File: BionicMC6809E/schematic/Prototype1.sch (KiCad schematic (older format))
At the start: 5 parts, among them J1 BionicConnector, U1 MC6809P, U2 74HCT126

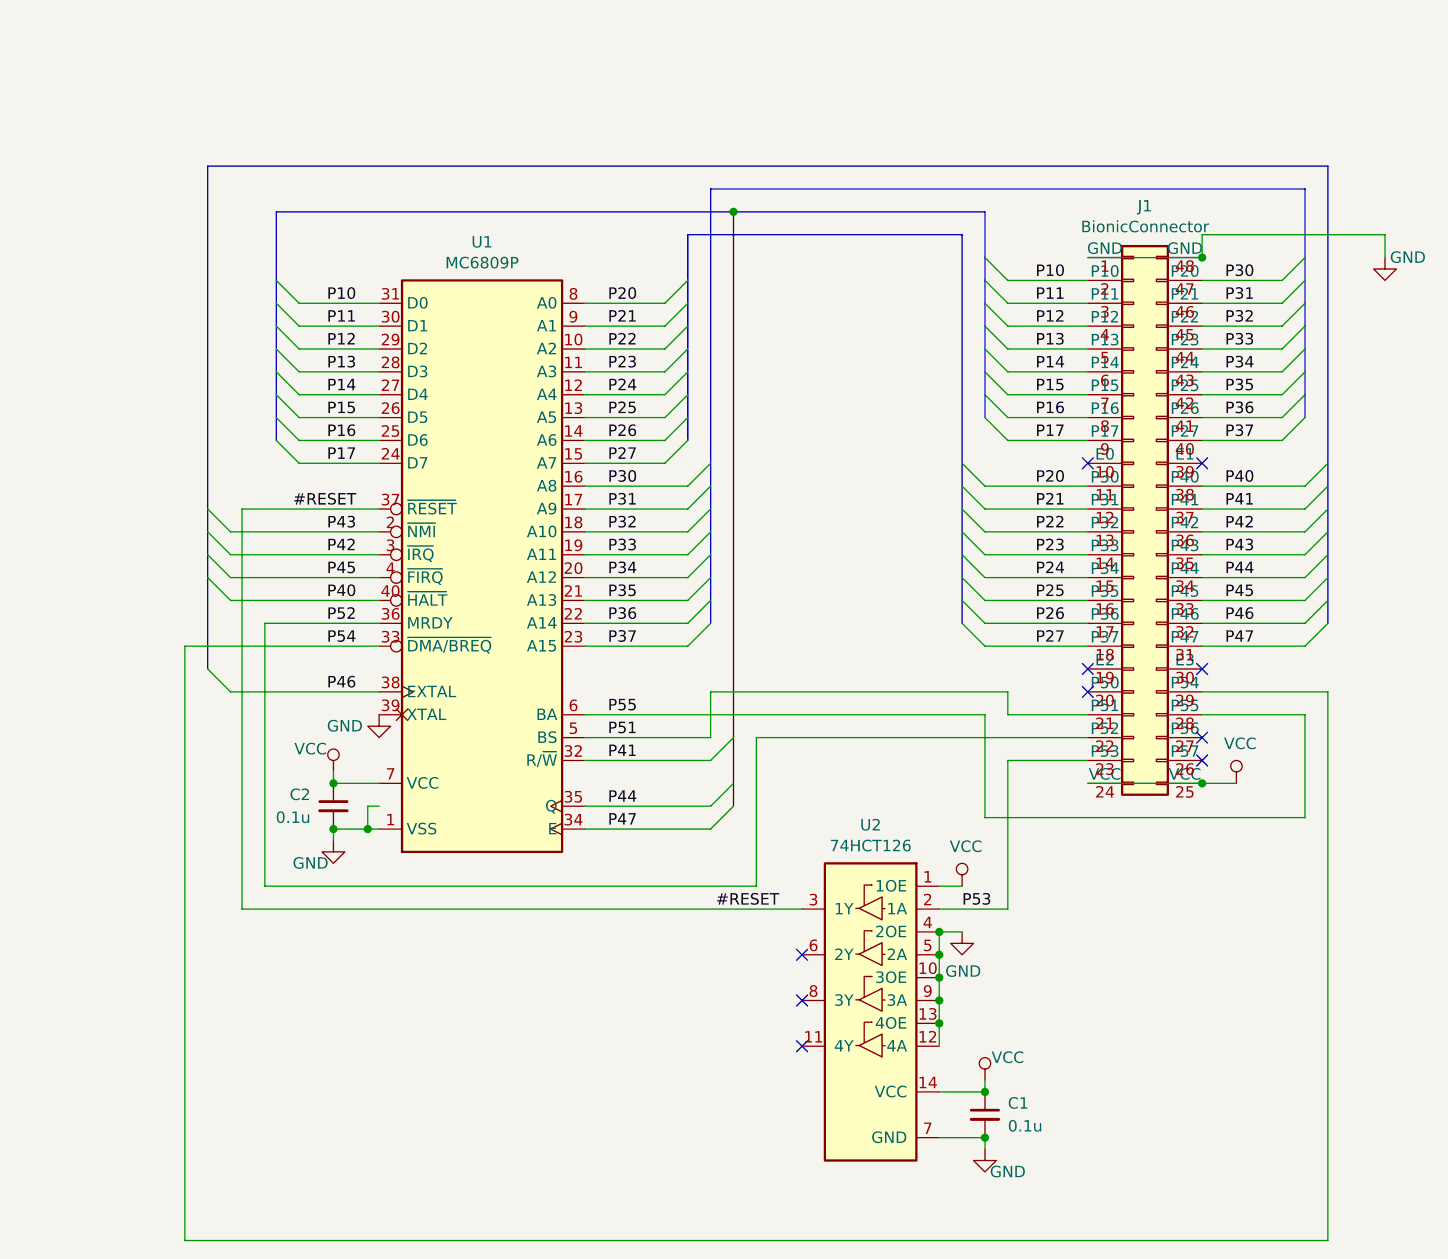
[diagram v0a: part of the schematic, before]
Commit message: [BionicMC6809E] Mezzanine board
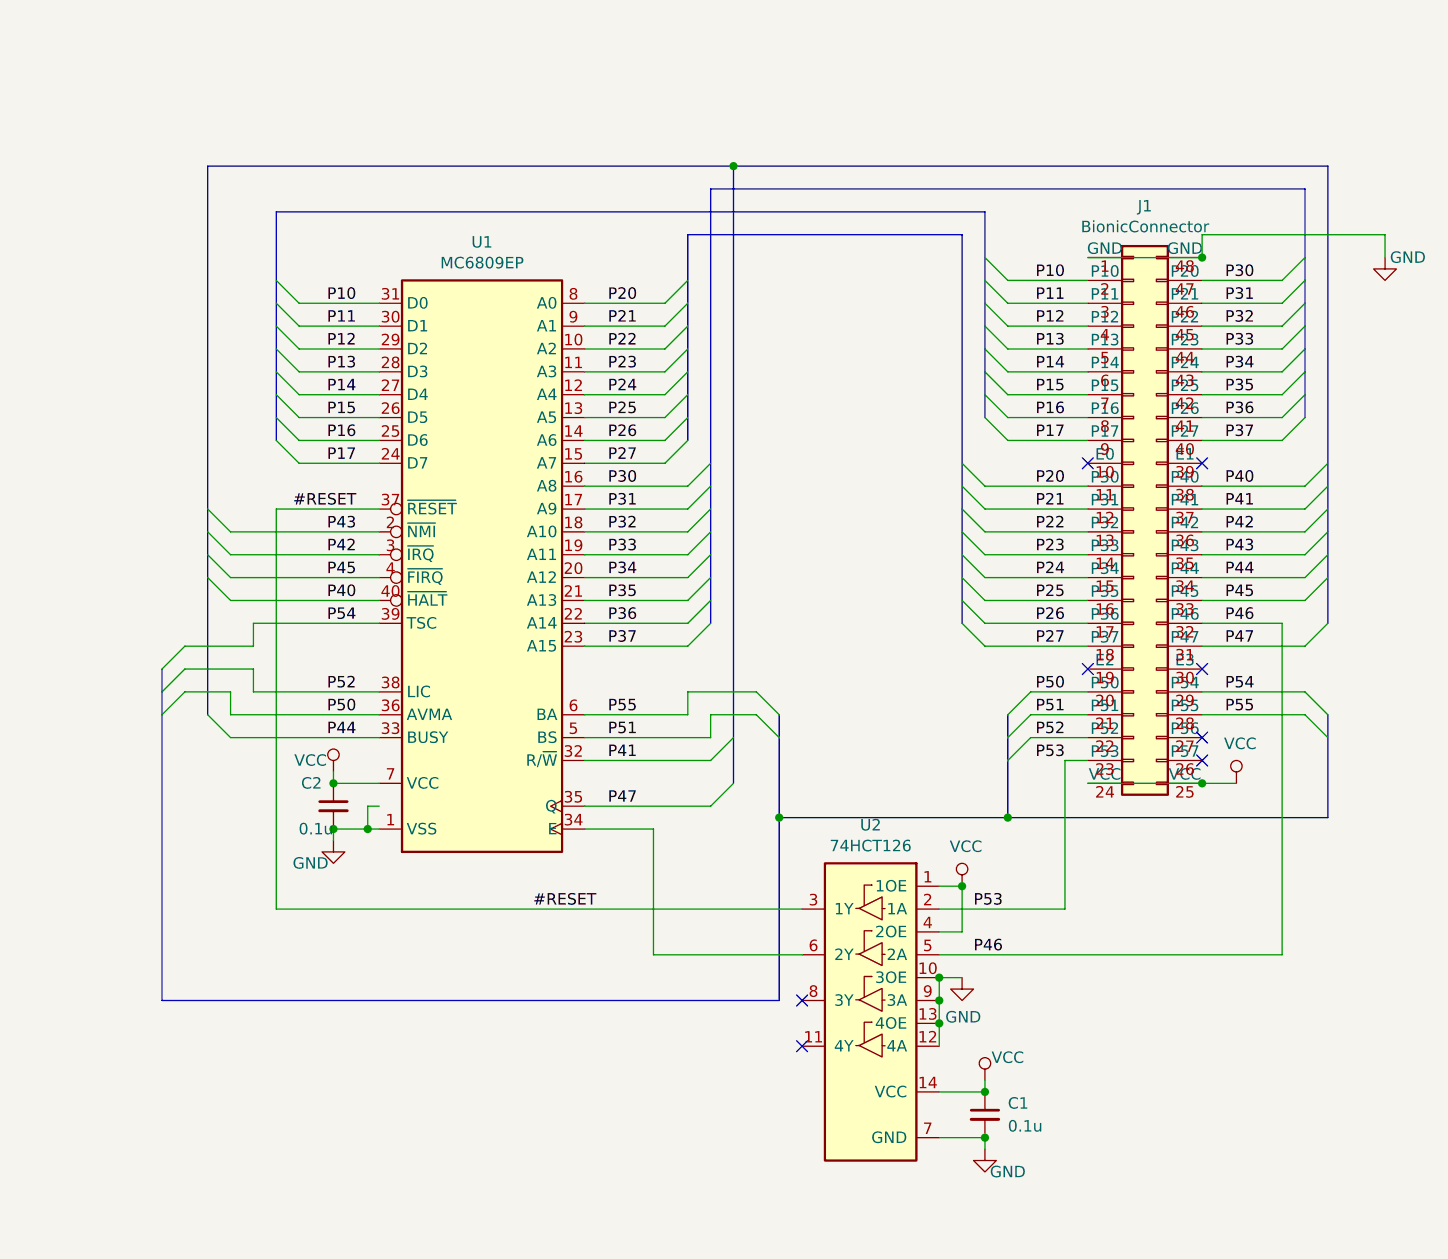
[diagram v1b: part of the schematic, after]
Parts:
- removed U1: MC6809P, Package_DIP:DIP-40_W15.24mm, symbol 0-LocalLibrary:MC6809P
- added U1: MC6809EP, Package_DIP:DIP-40_W15.24mm, symbol 0-LocalLibrary:MC6809EP
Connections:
- net #RESET: now also U1.37 (~RESET)
- net GND: now also U1.1 (VSS); no longer U2.4 (2OE), U2.5 (2A)
- net P10: now also U1.31 (D0)
- net P11: now also U1.30 (D1)
- net P12: now also U1.29 (D2)
- net P13: now also U1.28 (D3)
- net P14: now also U1.27 (D4)
- net P15: now also U1.26 (D5)
- net P16: now also U1.25 (D6)
- net P17: now also U1.24 (D7)
- net P20: now also U1.8 (A0)
- net P21: now also U1.9 (A1)
- net P22: now also U1.10 (A2)
- net P23: now also U1.11 (A3)
- net P24: now also U1.12 (A4)
- net P25: now also U1.13 (A5)
- net P26: now also U1.14 (A6)
- net P27: now also U1.15 (A7)
- net P30: now also U1.16 (A8)
- net P31: now also U1.17 (A9)
- net P32: now also U1.18 (A10)
- net P33: now also U1.19 (A11)
- net P34: now also U1.20 (A12)
- net P35: now also U1.21 (A13)
- net P36: now also U1.22 (A14)
- net P37: now also U1.23 (A15)
- net P40: now also U1.40 (~HALT)
- net P41: now also U1.32 (R/~W)
- net P42: now also U1.3 (~IRQ)
- net P43: now also U1.2 (~NMI)
- net P44: now also U1.33 (BUSY)
- net P45: now also U1.4 (~FIRQ)
- net P46: now also U2.5 (2A)
- net P47: now also U1.35 (Q)
- net P51: now also U1.5 (BS)
- net P52: now also U1.38 (LIC)
- net P54: now also U1.39 (TSC)
- net P55: now also U1.6 (BA)
- net VCC: now also U2.4 (2OE), U1.7 (VCC)
- net P50: now reaches J1.20 (P50)
- net P50: now also U1.36 (AVMA)
- net at U2.6 (2Y): now also U1.34 (E)
- no-connect marks 10 -> 8
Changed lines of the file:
@@
 encoding utf-8
 Sheet 1 1
-Title "BionicMC6809 Mezzanine"
-Date "2021-11-11"
+Title "BionicMC6809E Mezzanine"
+Date "2021-11-12"
 Rev "1"
 Comp "Tadashi G. Takaoka"
@@
 U 1 1 5D0E12B4
 P 3600 4200
-F 0 "C2" H 3700 4250 50  0000 L CNN
-F 1 "0.1u" H 3700 4150 50  0000 L CNN
+F 0 "C2" H 3650 4300 50  0000 L CNN
+F 1 "0.1u" H 3600 4100 50  0000 L CNN
 F 2 "Capacitor_THT:C_Disc_D3.4mm_W2.1mm_P2.50mm" H 3600 4200 50  0001 C CNN
 F 3 "~" H 3600 4200 50  0001 C CNN
@@
 P 3600 4050
 F 0 "#PWR03" H 3600 3900 50  0001 C CNN
-F 1 "VCC" H 3700 4150 50  0000 C CNN
+F 1 "VCC" H 3700 4100 50  0000 C CNN
 F 2 "" H 3600 4050 50  0001 C CNN
 F 3 "" H 3600 4050 50  0001 C CNN
@@
 Wire Wire Line
 	7750 2600 7400 2600
-Text Label 6350 4650 0    50   ~ 0
+Text Label 6400 4650 0    50   ~ 0
 P53
 Text Label 3700 3000 2    50   ~ 0
@@
 	1    0    0    -1
 $EndComp
-NoConn ~ 5650 4850
 NoConn ~ 5650 5050
 NoConn ~ 5650 5250
-Text Label 5550 4650 2    50   ~ 0
+Text Label 4750 4650 2    50   ~ 0
 #RESET
 Text Label 3700 2900 2    50   ~ 0
@@
 Entry Wire Line
 	5350 4100 5250 4200
-Entry Wire Line
-	5350 4200 5250 4300
 Text Label 7500 2800 0    50   ~ 0
 P40
@@
 	7400 3300 7850 3300
 Wire Wire Line
-	7400 3400 7850 3400
-Wire Wire Line
 	7400 3500 7850 3500
 Entry Wire Line
@@
 	7950 3200 7850 3300
 Entry Wire Line
-	7950 3300 7850 3400
-Entry Wire Line
 	7950 3400 7850 3500
-Wire Wire Line
-	6900 4000 6550 4000
-Wire Wire Line
-	6550 4650 6250 4650
-Wire Wire Line
-	6250 4750 6350 4750
 $Comp
 L power:GND #PWR06
 U 1 1 61A0F5E3
-P 6350 4750
-F 0 "#PWR06" H 6350 4500 50  0001 C CNN
-F 1 "GND" H 6355 4577 50  0000 C CNN
-F 2 "" H 6350 4750 50  0001 C CNN
-F 3 "" H 6350 4750 50  0001 C CNN
-	1    6350 4750
+P 6350 4950
+F 0 "#PWR06" H 6350 4700 50  0001 C CNN
+F 1 "GND" H 6355 4777 50  0000 C CNN
+F 2 "" H 6350 4950 50  0001 C CNN
+F 3 "" H 6350 4950 50  0001 C CNN
+	1    6350 4950
 	1    0    0    -1
 $EndComp
@@
 Wire Wire Line
 	3150 3100 3800 3100
-Wire Wire Line
-	6250 4750 6250 4850
 $Comp
 L 0-LocalLibrary:BionicConnector J1
@@
 	-1   0    0    -1
 $EndComp
-Connection ~ 6250 4750
 Wire Wire Line
 	3150 3000 3800 3000
@@
 Entry Wire Line
 	3050 3100 3150 3200
-Wire Bus Line
-	3350 1600 5350 1600
 Wire Bus Line
 	5150 1700 6350 1700
@@
 P55
 Text Label 4800 4200 0    50   ~ 0
-P44
-Text Label 4800 4300 0    50   ~ 0
 P47
+Wire Wire Line
+	5250 4200 4700 4200
 Text Label 3700 3700 2    50   ~ 0
-P46
-Wire Wire Line
-	3150 3700 3800 3700
-Entry Wire Line
-	3050 3600 3150 3700
-Wire Bus Line
-	3050 1400 7950 1400
-Connection ~ 5350 1600
-Wire Bus Line
-	5350 1600 6450 1600
-Wire Wire Line
-	4700 4300 5250 4300
-Wire Wire Line
-	5250 4200 4700 4200
-Text Label 3700 3400 2    50   ~ 0
 P52
 Connection ~ 7400 1800
@@
 Connection ~ 7400 4100
 Wire Wire Line
-	6900 3900 5450 3900
-Wire Wire Line
-	5450 3900 5450 4550
-Wire Wire Line
-	5450 4550 3300 4550
-Wire Wire Line
-	3300 4550 3300 3400
-Wire Wire Line
-	3300 3400 3800 3400
-Wire Wire Line
-	3200 4650 3200 2900
-Wire Wire Line
-	3200 2900 3800 2900
-Wire Wire Line
-	3200 4650 5650 4650
-Wire Wire Line
 	6250 5250 6250 5150
-Connection ~ 6250 4850
-Connection ~ 6250 4950
-Wire Wire Line
-	6250 4950 6250 4850
 Connection ~ 6250 5050
 Wire Wire Line
@@
 	6250 5150 6250 5050
 Wire Wire Line
-	4700 3800 6450 3800
-Wire Wire Line
-	7850 3800 7400 3800
-Wire Wire Line
-	6550 4000 6550 4650
-Wire Wire Line
-	7850 3800 7850 4250
-$Comp
-L power:GND #PWR0103
-U 1 1 61B28763
-P 3800 3800
-F 0 "#PWR0103" H 3800 3550 50  0001 C CNN
-F 1 "GND" H 3650 3750 50  0000 C CNN
-F 2 "" H 3800 3800 50  0001 C CNN
-F 3 "" H 3800 3800 50  0001 C CNN
-	1    3800 3800
-	1    0    0    -1
-$EndComp
-$Comp
-L 0-LocalLibrary:MC6809P U1
-U 1 1 61B48BA8
-P 4250 3100
-F 0 "U1" H 4250 4467 50  0000 C CNN
-F 1 "MC6809P" H 4250 4376 50  0000 C CNN
-F 2 "Package_DIP:DIP-40_W15.24mm" H 4300 1750 50  0001 C CIN
-F 3 "https://pdf1.alldatasheet.jp/datasheet-pdf/view/4143/MOTOROLA/MC6809.html" H 4250 3100 50  0001 C CNN
-	1    4250 3100
-	1    0    0    -1
-$EndComp
+	6800 4000 6800 4650
 Wire Wire Line
 	3800 3300 3150 3300
@@
 Text Label 3700 3300 2    50   ~ 0
 P40
-NoConn ~ 6900 3700
-Wire Wire Line
-	6450 3800 6450 4250
-Wire Wire Line
-	6900 3800 6550 3800
-Wire Wire Line
-	6550 3800 6550 3700
-Wire Wire Line
-	6550 3700 5250 3700
-Wire Wire Line
-	5250 3700 5250 3900
-Wire Wire Line
-	5250 3900 4700 3900
 Text Label 4800 3900 0    50   ~ 0
 P51
@@
 Text Label 4800 4000 0    50   ~ 0
 P41
-Wire Wire Line
-	7950 3700 7950 6100
-Wire Wire Line
-	7950 6100 2950 6100
-Wire Wire Line
-	2950 6100 2950 3500
-Text Label 3700 3500 2    50   ~ 0
+Text Label 3700 3400 2    50   ~ 0
 P54
-Wire Wire Line
-	6450 4250 7850 4250
-Wire Wire Line
-	7400 3700 7950 3700
-Wire Wire Line
-	2950 3500 3800 3500
-Wire Bus Line
-	5350 1600 5350 4200
-Wire Bus Line
-	3050 1400 3050 3600
+$Comp
+L 0-LocalLibrary:MC6809EP U1
+U 1 1 61C84FCF
+P 4250 3100
+F 0 "U1" H 4250 4467 50  0000 C CNN
+F 1 "MC6809EP" H 4250 4376 50  0000 C CNN
+F 2 "Package_DIP:DIP-40_W15.24mm" H 4250 1750 50  0001 C CNN
+F 3 "https://colorcomputerarchive.com/repo/Documents/Datasheets/MC6809E%20HMOS%208%20Bit%20Microprocessor%20(Motorola).pdf" H 4150 4525 50  0001 C CNN
+	1    4250 3100
+	1    0    0    -1
+$EndComp
+Wire Wire Line
+	6250 4950 6350 4950
+Connection ~ 6250 4950
+Wire Wire Line
+	6350 4750 6250 4750
+Connection ~ 6350 4550
+Wire Wire Line
+	6350 4550 6350 4750
+Wire Wire Line
+	7400 3400 7750 3400
+Wire Wire Line
+	7750 3400 7750 4850
+Wire Wire Line
+	7750 4850 6250 4850
+Text Label 6400 4850 0    50   ~ 0
+P46
+Wire Wire Line
+	4700 4300 5000 4300
+Wire Wire Line
+	5000 4300 5000 4850
+Wire Wire Line
+	5000 4850 5650 4850
+Wire Bus Line
+	3350 1600 6450 1600
+Wire Bus Line
+	3050 1400 5350 1400
+Connection ~ 5350 1400
+Wire Bus Line
+	5350 1400 7950 1400
+Entry Wire Line
+	3150 3900 3050 3800
+Wire Wire Line
+	3800 3900 3150 3900
+Wire Wire Line
+	3350 2900 3350 4650
+Wire Wire Line
+	3350 2900 3800 2900
+Wire Wire Line
+	3350 4650 5650 4650
+Text Label 3700 3800 2    50   ~ 0
+P50
+Text Label 3700 3900 2    50   ~ 0
+P44
+Entry Wire Line
+	2850 3700 2950 3600
+Entry Wire Line
+	2850 3800 2950 3700
+Entry Wire Line
+	2850 3600 2950 3500
+Wire Wire Line
+	2950 3500 3250 3500
+Wire Wire Line
+	2950 3600 3250 3600
+Entry Wire Line
+	5550 3800 5450 3700
+Entry Wire Line
+	5550 3900 5450 3800
+Wire Wire Line
+	5250 3800 5250 3900
+Wire Wire Line
+	5250 3900 4700 3900
+Wire Wire Line
+	5250 3800 5450 3800
+Wire Wire Line
+	5150 3700 5150 3800
+Wire Wire Line
+	5150 3800 4700 3800
+Wire Wire Line
+	5150 3700 5450 3700
+Wire Wire Line
+	2950 3700 3150 3700
+Wire Wire Line
+	3150 3700 3150 3800
+Wire Wire Line
+	3150 3800 3800 3800
+Wire Wire Line
+	3250 3600 3250 3700
+Wire Wire Line
+	3250 3700 3800 3700
+Wire Wire Line
+	3250 3500 3250 3400
+Wire Wire Line
+	3250 3400 3800 3400
+Wire Wire Line
+	7400 3700 7850 3700
+Wire Wire Line
+	7400 3800 7850 3800
+Entry Wire Line
+	7850 3800 7950 3900
+Entry Wire Line
+	7850 3700 7950 3800
+Text Label 7500 3700 0    50   ~ 0
+P54
+Text Label 7500 3800 0    50   ~ 0
+P55
+Text Label 6800 3700 2    50   ~ 0
+P50
+Text Label 6800 3800 2    50   ~ 0
+P51
+Text Label 6800 3900 2    50   ~ 0
+P52
+Text Label 6800 4000 2    50   ~ 0
+P53
+Wire Wire Line
+	6800 4000 6900 4000
+Wire Wire Line
+	6250 4650 6800 4650
+Entry Wire Line
+	6550 3800 6650 3700
+Entry Wire Line
+	6550 3900 6650 3800
+Entry Wire Line
+	6550 4000 6650 3900
+Wire Wire Line
+	6900 3700 6650 3700
+Wire Wire Line
+	6900 3800 6650 3800
+Wire Wire Line
+	6900 3900 6650 3900
+Wire Bus Line
+	7950 4250 6550 4250
+Connection ~ 6550 4250
+Wire Bus Line
+	6550 4250 5550 4250
+Wire Bus Line
+	5550 4250 5550 5050
+Wire Bus Line
+	5550 5050 2850 5050
+Wire Bus Line
+	5350 1400 5350 4100
+Wire Bus Line
+	7950 3800 7950 4250
+Wire Bus Line
+	5550 3800 5550 4250
+Wire Bus Line
+	2850 3600 2850 5050
+Wire Bus Line
+	6550 3800 6550 4250
+Wire Bus Line
+	3050 1400 3050 3800
+Wire Bus Line
+	7950 1400 7950 3400
 Wire Bus Line
 	5250 1500 5250 3400
 Wire Bus Line
-	7950 1400 7950 3400
-Wire Bus Line
 	7850 1500 7850 2500
 Wire Bus Line
@@
 Wire Bus Line
 	3350 1600 3350 2600
+Connection ~ 5550 4250
 $EndSCHEMATC
